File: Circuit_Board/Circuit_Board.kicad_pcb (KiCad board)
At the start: 4 copper layers, 86 x 70.5 mm, 43 parts, among them J1 Conn_01x02, J2 Control stuff, J3 Power stuff, J4 Conn_02x06_Odd_Even, J5 Conn_01x20_Socket, J6 Conn_01x20_Socket, J7 GPIO_1, J8 GPIO_2, J9 LED_AMP, Q2 IRF540N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

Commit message: update PCB with proper silkscreen value for IR LED
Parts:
- R4: value 100k -> 100R
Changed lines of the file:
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@@
 			)
 		)
-		(property "Value" "100k"
+		(property "Value" "100R"
 			(at 0.0875 1.5 90)
 			(layer "F.SilkS")

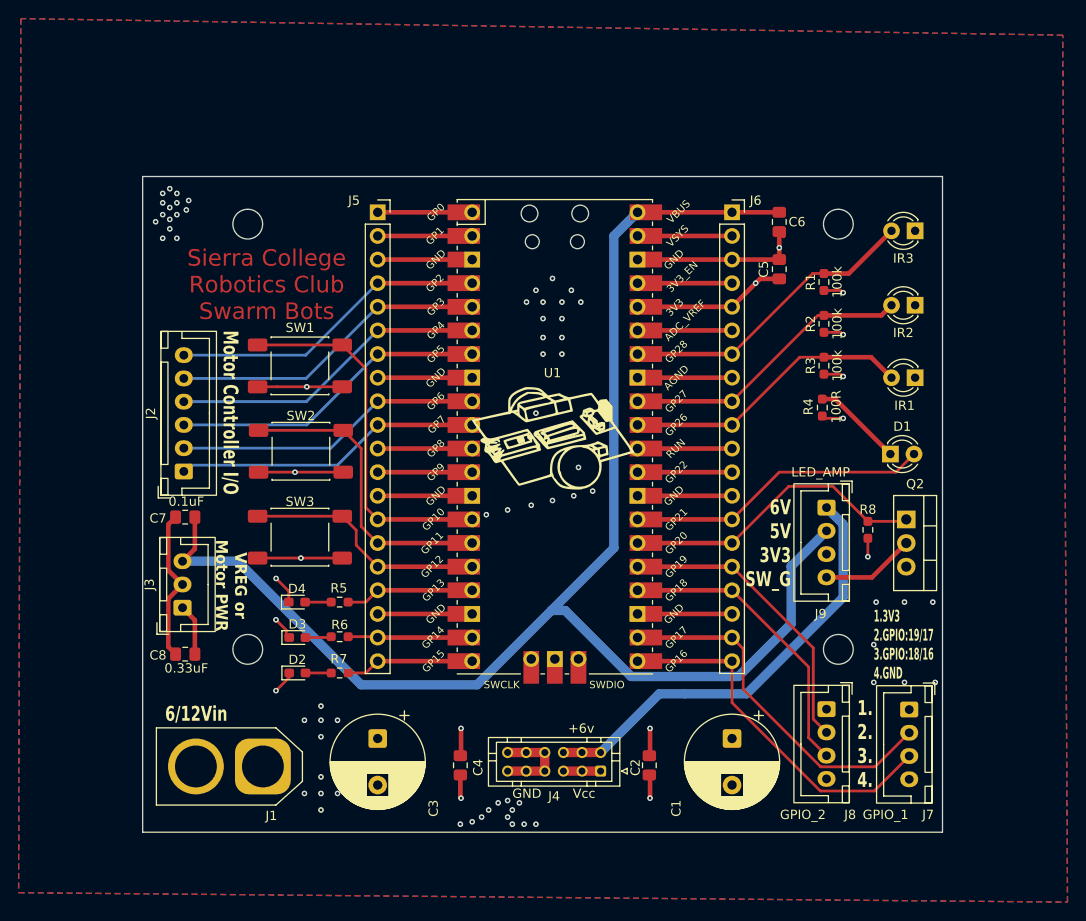
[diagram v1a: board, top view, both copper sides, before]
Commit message: Updated component values
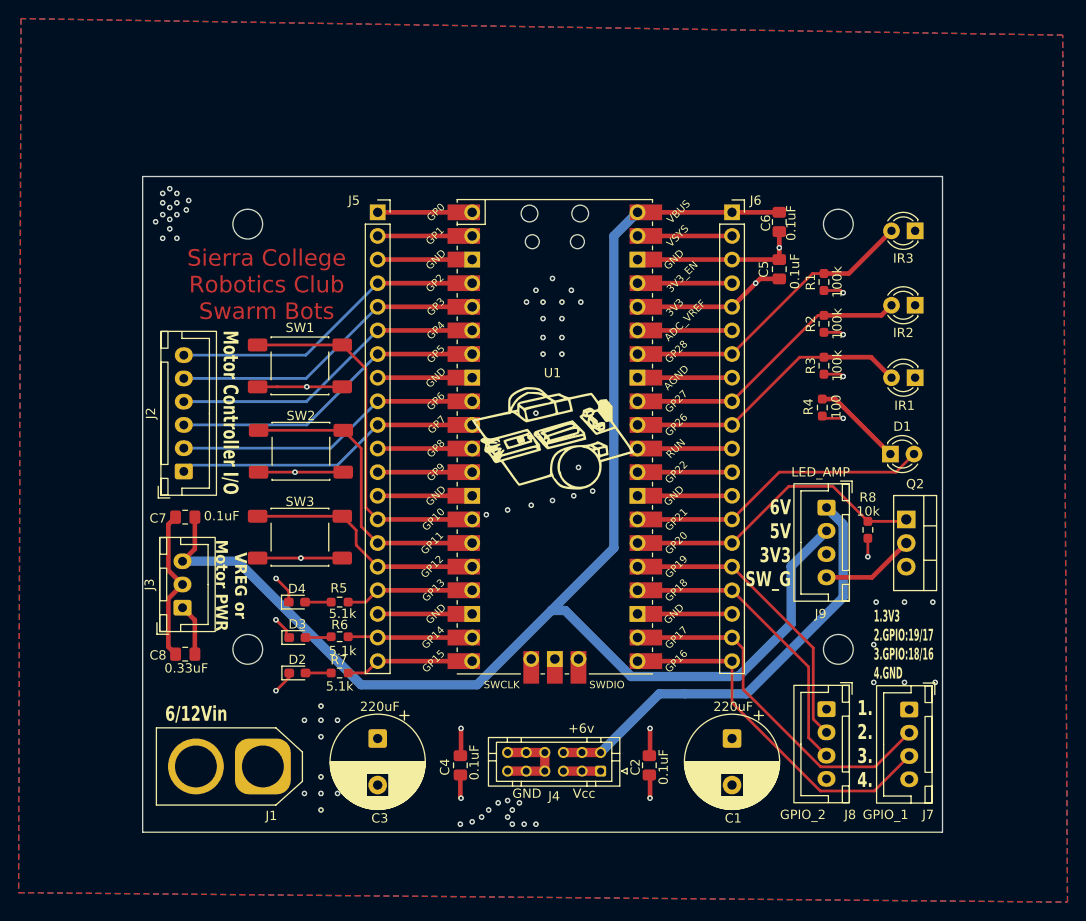
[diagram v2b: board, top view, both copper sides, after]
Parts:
- C1, C3: value C_Polarized -> 220uF
- C2, C4, C5, C6: value C_Polarized -> 0.1uF
- R4: value 100R -> 100
- R5, R6, R7: value R -> 5.1k
- R8: value R -> 10k
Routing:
- net GND: track 115.2 -> 114.5 mm
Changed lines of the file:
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@@
 		(tags "resistor handsolder")
 		(property "Reference" "R8"
-			(at 2.1825 0 180)
+			(at 3.4895 0 180)
 			(layer "F.SilkS")
 			(effects
@@
 			)
 		)
-		(property "Value" "R"
-			(at 0 1.43 90)
-			(layer "F.Fab")
+		(property "Value" "10k"
+			(at 1.9895 0.025 180)
+			(layer "F.SilkS")
 			(effects
 				(font
@@
 		(tags "CP Radial series Radial pin pitch 5.00mm diameter 10mm height 16mm Electrolytic Capacitor")
 		(property "Reference" "C3"
-			(at 7.5 -6 90)
+			(at 8.57 -0.23 180)
 			(layer "F.SilkS")
 			(effects
@@
 			)
 		)
-		(property "Value" "C_Polarized"
-			(at 1.867677 -6 90)
-			(layer "F.Fab")
+		(property "Value" "220uF"
+			(at -3.43 -0.23 180)
+			(layer "F.SilkS")
 			(effects
 				(font
@@
 		(tags "capacitor handsolder")
 		(property "Reference" "C6"
-			(at 0 -1.905 180)
+			(at 0.1125 1.45 90)
 			(layer "F.SilkS")
 			(effects
@@
 			)
 		)
-		(property "Value" "C_Polarized"
-			(at 2.7725 -1.27 90)
-			(layer "F.Fab")
-			(hide yes)
+		(property "Value" "0.1uF"
+			(at 0.1125 -1.27 90)
+			(layer "F.SilkS")
 			(effects
 				(font
@@
 		)
 		(property "Value" "MountingHole"
-			(at 0 4.15 0)
+			(at 1.2 3.88 0)
 			(layer "F.Fab")
 			(effects
@@
 		(tags "capacitor handsolder")
 		(property "Reference" "C4"
-			(at 0.2325 -1.905 90)
+			(at 0.1925 1.66 90)
 			(layer "F.SilkS")
 			(effects
@@
 			)
 		)
-		(property "Value" "C_Polarized"
-			(at -0.5 -1.5 90)
-			(layer "F.Fab")
-			(hide yes)
+		(property "Value" "0.1uF"
+			(at -0.3075 -1.5 90)
+			(layer "F.SilkS")
 			(effects
 				(font
@@
 		(tags "capacitor handsolder")
 		(property "Reference" "C2"
-			(at 0.2325 1.5 90)
+			(at 0.1925 1.5 90)
 			(layer "F.SilkS")
 			(effects
@@
 			)
 		)
-		(property "Value" "C_Polarized"
-			(at -0.5 1.68 90)
-			(layer "F.Fab")
-			(hide yes)
+		(property "Value" "0.1uF"
+			(at 0.1925 -1.52 90)
+			(layer "F.SilkS")
 			(effects
 				(font
@@
 		)
 		(property "Value" "0.1uF"
-			(at -0.11975 1.68 0)
+			(at -3.92375 0.12425 0)
 			(layer "F.SilkS")
 			(effects
@@
 			)
 		)
-		(property "Value" "R"
-			(at 0 1.43 0)
-			(layer "F.Fab")
-			(hide yes)
+		(property "Value" "5.1k"
+			(at 0.3175 1.52 0)
+			(layer "F.SilkS")
 			(effects
 				(font
@@
 		(tags "resistor handsolder")
 		(property "Reference" "R7"
-			(at -0.0875 -1.5 0)
+			(at -0.0875 -1.38 0)
 			(layer "F.SilkS")
 			(effects
@@
 			)
 		)
-		(property "Value" "R"
+		(property "Value" "5.1k"
 			(at 0 1.43 0)
-			(layer "F.Fab")
-			(hide yes)
+			(layer "F.SilkS")
 			(effects
 				(font
@@
 			)
 		)
-		(property "Value" "C_Polarized"
+		(property "Value" "0.1uF"
 			(at -0.2325 1.68 90)
-			(layer "F.Fab")
-			(hide yes)
+			(layer "F.SilkS")
 			(effects
 				(font
@@
 		(tags "CP Radial series Radial pin pitch 5.00mm diameter 10mm height 16mm Electrolytic Capacitor")
 		(property "Reference" "C1"
-			(at 7.5 6 90)
+			(at 8.57 -0.13 180)
 			(layer "F.SilkS")
 			(effects
@@
 			)
 		)
-		(property "Value" "C_Polarized"
-			(at 2.5 6 90)
-			(layer "F.Fab")
+		(property "Value" "220uF"
+			(at -3.43 -0.13 180)
+			(layer "F.SilkS")
 			(effects
 				(font
@@
 			)
 		)
-		(property "Value" "R"
-			(at 0 1.43 0)
-			(layer "F.Fab")
-			(hide yes)
+		(property "Value" "5.1k"
+			(at 0.3175 1.24 0)
+			(layer "F.SilkS")
 			(effects
 				(font
@@
 			)
 		)
-		(property "Value" "100R"
+		(property "Value" "100"
 			(at 0.0875 1.5 90)
 			(layer "F.SilkS")
@@
 		(layer "F.Cu")
 		(net "GND")
-	)
-	(segment
-		(start 171.915 72.39)
-		(end 171.45 71.925)
-		(width 0.5)
-		(layer "F.Cu")
-		(net "GND")
